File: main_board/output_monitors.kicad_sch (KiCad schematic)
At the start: 52 parts, among them U14 TL072CDR, U17 TL072CDR, U18 TL072CDR, U4 TL072CDR

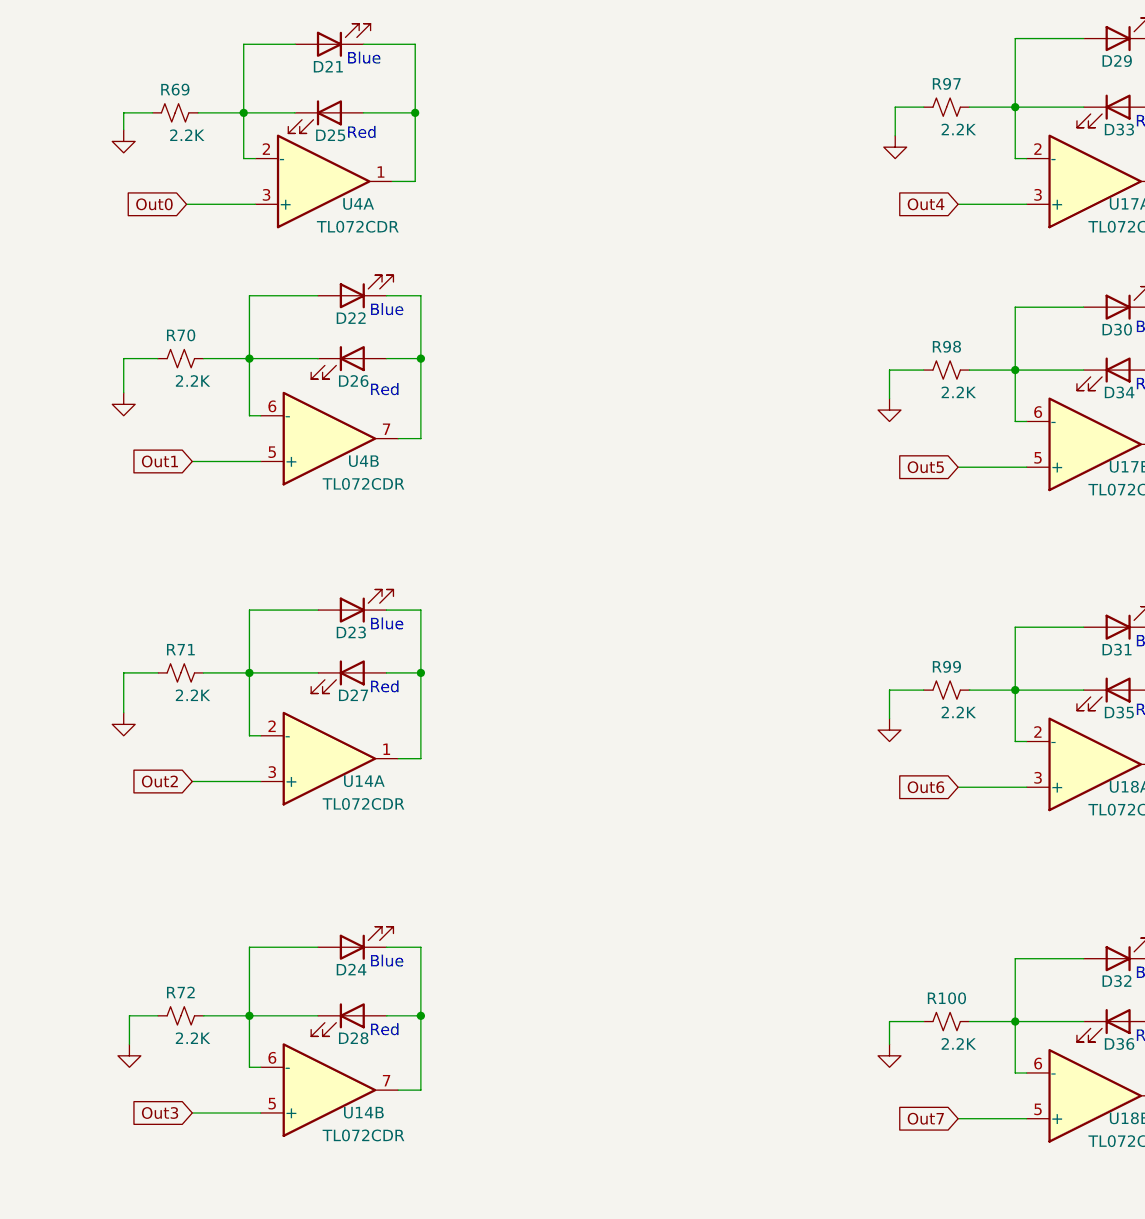
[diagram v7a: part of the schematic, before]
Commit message: Fixes main board.
Fixes regulator footprint. Re lays out board to improve noise performance. Around -50db now at outputs.
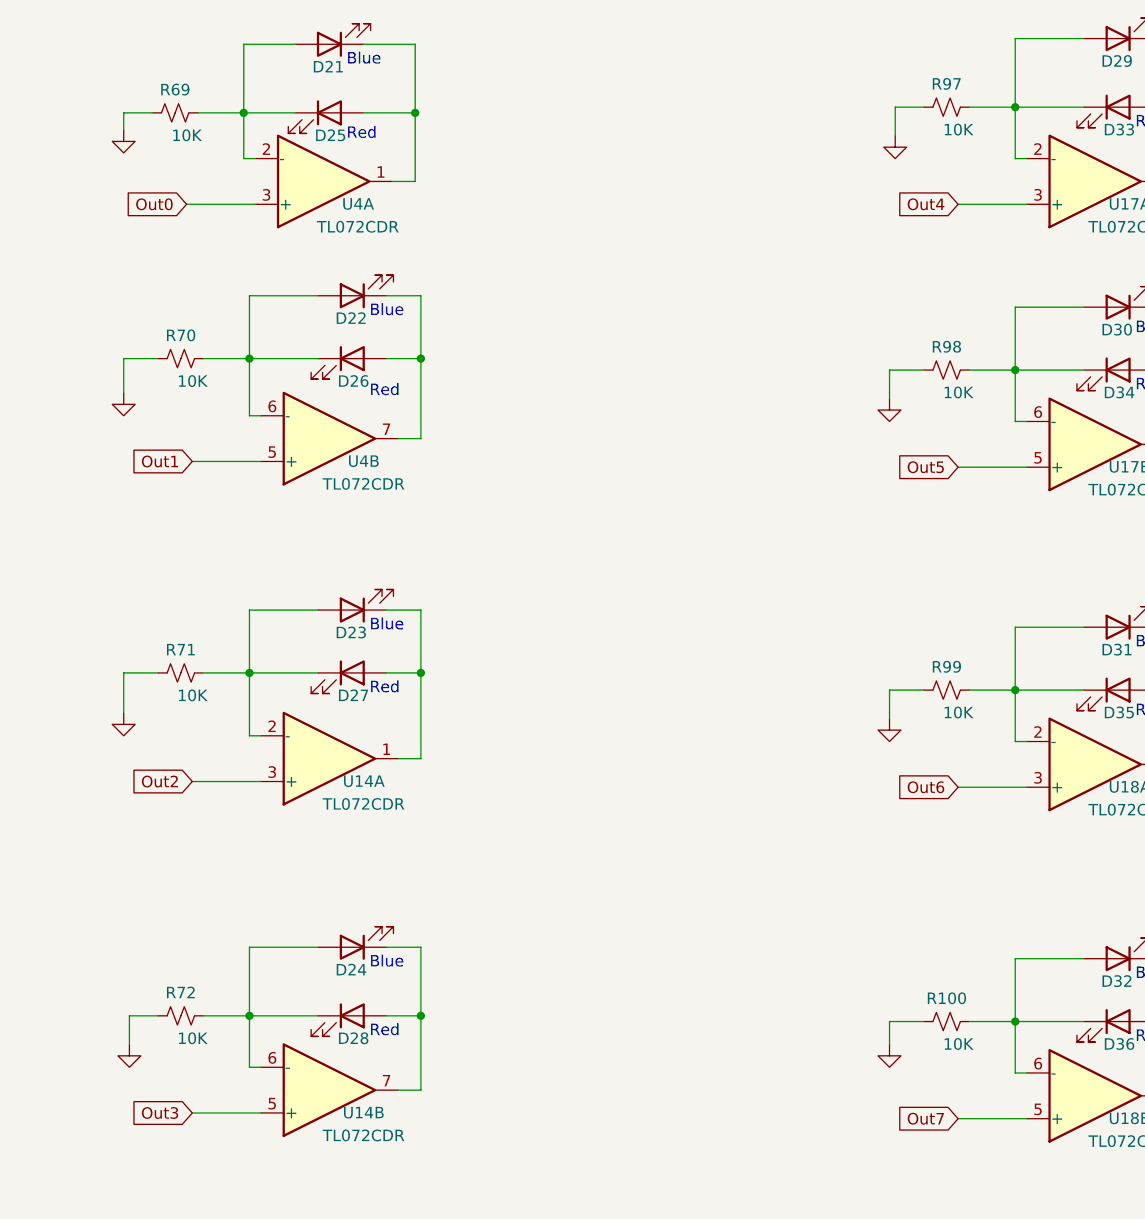
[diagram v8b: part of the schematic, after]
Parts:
- R100, R69, R70, R71, R72, R97, R98, R99: value 2.2K -> 10K; Digi-Key Part 311-10KARCT-ND -> 13-RC0805JR-1010KLCT-ND; LCSC Part # C17520 -> C17414
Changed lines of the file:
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@@
     (in_bom yes) (on_board yes)
     (property "Reference" "R72" (id 0) (at 79.375 125.095 90))
-    (property "Value" "2.2K" (id 1) (at 80.645 130.175 90))
+    (property "Value" "10K" (id 1) (at 80.645 130.175 90))
     (property "Footprint" "Resistor_SMD:R_0805_2012Metric_Pad1.20x1.40mm_HandSolder" (id 2) (at 79.375 127.635 0)
       (effects (font (size 1.27 1.27)) hide)
@@
       (effects (font (size 1.27 1.27)) hide)
     )
-    (property "Digi-Key Part" "311-10KARCT-ND" (id 4) (at 79.375 127.635 90)
-      (effects (font (size 1.27 1.27)) hide)
-    )
-    (property "LCSC Part #" "C17520" (id 5) (at 79.375 127.635 0)
+    (property "Digi-Key Part" "13-RC0805JR-1010KLCT-ND" (id 4) (at 79.375 127.635 90)
+      (effects (font (size 1.27 1.27)) hide)
+    )
+    (property "LCSC Part #" "C17414" (id 5) (at 79.375 127.635 0)
       (effects (font (size 1.27 1.27)) hide)
     )
@@
     (in_bom yes) (on_board yes)
     (property "Reference" "R100" (id 0) (at 164.465 125.73 90))
-    (property "Value" "2.2K" (id 1) (at 165.735 130.81 90))
+    (property "Value" "10K" (id 1) (at 165.735 130.81 90))
     (property "Footprint" "Resistor_SMD:R_0805_2012Metric_Pad1.20x1.40mm_HandSolder" (id 2) (at 164.465 128.27 0)
       (effects (font (size 1.27 1.27)) hide)
@@
       (effects (font (size 1.27 1.27)) hide)
     )
-    (property "Digi-Key Part" "311-10KARCT-ND" (id 4) (at 164.465 128.27 90)
-      (effects (font (size 1.27 1.27)) hide)
-    )
-    (property "LCSC Part #" "C17520" (id 5) (at 164.465 128.27 0)
+    (property "Digi-Key Part" "13-RC0805JR-1010KLCT-ND" (id 4) (at 164.465 128.27 90)
+      (effects (font (size 1.27 1.27)) hide)
+    )
+    (property "LCSC Part #" "C17414" (id 5) (at 164.465 128.27 0)
       (effects (font (size 1.27 1.27)) hide)
     )
@@
     (in_bom yes) (on_board yes)
     (property "Reference" "R69" (id 0) (at 78.74 24.765 90))
-    (property "Value" "2.2K" (id 1) (at 80.01 29.845 90))
+    (property "Value" "10K" (id 1) (at 80.01 29.845 90))
     (property "Footprint" "Resistor_SMD:R_0805_2012Metric_Pad1.20x1.40mm_HandSolder" (id 2) (at 78.74 27.305 0)
       (effects (font (size 1.27 1.27)) hide)
@@
       (effects (font (size 1.27 1.27)) hide)
     )
-    (property "Digi-Key Part" "311-10KARCT-ND" (id 4) (at 78.74 27.305 90)
-      (effects (font (size 1.27 1.27)) hide)
-    )
-    (property "LCSC Part #" "C17520" (id 5) (at 78.74 27.305 0)
+    (property "Digi-Key Part" "13-RC0805JR-1010KLCT-ND" (id 4) (at 78.74 27.305 90)
+      (effects (font (size 1.27 1.27)) hide)
+    )
+    (property "LCSC Part #" "C17414" (id 5) (at 78.74 27.305 0)
       (effects (font (size 1.27 1.27)) hide)
     )
@@
     (in_bom yes) (on_board yes)
     (property "Reference" "R99" (id 0) (at 164.465 88.9 90))
-    (property "Value" "2.2K" (id 1) (at 165.735 93.98 90))
+    (property "Value" "10K" (id 1) (at 165.735 93.98 90))
     (property "Footprint" "Resistor_SMD:R_0805_2012Metric_Pad1.20x1.40mm_HandSolder" (id 2) (at 164.465 91.44 0)
       (effects (font (size 1.27 1.27)) hide)
@@
       (effects (font (size 1.27 1.27)) hide)
     )
-    (property "Digi-Key Part" "311-10KARCT-ND" (id 4) (at 164.465 91.44 90)
-      (effects (font (size 1.27 1.27)) hide)
-    )
-    (property "LCSC Part #" "C17520" (id 5) (at 164.465 91.44 0)
+    (property "Digi-Key Part" "13-RC0805JR-1010KLCT-ND" (id 4) (at 164.465 91.44 90)
+      (effects (font (size 1.27 1.27)) hide)
+    )
+    (property "LCSC Part #" "C17414" (id 5) (at 164.465 91.44 0)
       (effects (font (size 1.27 1.27)) hide)
     )
@@
     (in_bom yes) (on_board yes)
     (property "Reference" "R98" (id 0) (at 164.465 53.34 90))
-    (property "Value" "2.2K" (id 1) (at 165.735 58.42 90))
+    (property "Value" "10K" (id 1) (at 165.735 58.42 90))
     (property "Footprint" "Resistor_SMD:R_0805_2012Metric_Pad1.20x1.40mm_HandSolder" (id 2) (at 164.465 55.88 0)
       (effects (font (size 1.27 1.27)) hide)
@@
       (effects (font (size 1.27 1.27)) hide)
     )
-    (property "Digi-Key Part" "311-10KARCT-ND" (id 4) (at 164.465 55.88 90)
-      (effects (font (size 1.27 1.27)) hide)
-    )
-    (property "LCSC Part #" "C17520" (id 5) (at 164.465 55.88 0)
+    (property "Digi-Key Part" "13-RC0805JR-1010KLCT-ND" (id 4) (at 164.465 55.88 90)
+      (effects (font (size 1.27 1.27)) hide)
+    )
+    (property "LCSC Part #" "C17414" (id 5) (at 164.465 55.88 0)
       (effects (font (size 1.27 1.27)) hide)
     )
@@
     (in_bom yes) (on_board yes)
     (property "Reference" "R70" (id 0) (at 79.375 52.07 90))
-    (property "Value" "2.2K" (id 1) (at 80.645 57.15 90))
+    (property "Value" "10K" (id 1) (at 80.645 57.15 90))
     (property "Footprint" "Resistor_SMD:R_0805_2012Metric_Pad1.20x1.40mm_HandSolder" (id 2) (at 79.375 54.61 0)
       (effects (font (size 1.27 1.27)) hide)
@@
       (effects (font (size 1.27 1.27)) hide)
     )
-    (property "Digi-Key Part" "311-10KARCT-ND" (id 4) (at 79.375 54.61 90)
-      (effects (font (size 1.27 1.27)) hide)
-    )
-    (property "LCSC Part #" "C17520" (id 5) (at 79.375 54.61 0)
+    (property "Digi-Key Part" "13-RC0805JR-1010KLCT-ND" (id 4) (at 79.375 54.61 90)
+      (effects (font (size 1.27 1.27)) hide)
+    )
+    (property "LCSC Part #" "C17414" (id 5) (at 79.375 54.61 0)
       (effects (font (size 1.27 1.27)) hide)
     )
@@
     (in_bom yes) (on_board yes)
     (property "Reference" "R71" (id 0) (at 79.375 86.995 90))
-    (property "Value" "2.2K" (id 1) (at 80.645 92.075 90))
+    (property "Value" "10K" (id 1) (at 80.645 92.075 90))
     (property "Footprint" "Resistor_SMD:R_0805_2012Metric_Pad1.20x1.40mm_HandSolder" (id 2) (at 79.375 89.535 0)
       (effects (font (size 1.27 1.27)) hide)
@@
       (effects (font (size 1.27 1.27)) hide)
     )
-    (property "Digi-Key Part" "311-10KARCT-ND" (id 4) (at 79.375 89.535 90)
-      (effects (font (size 1.27 1.27)) hide)
-    )
-    (property "LCSC Part #" "C17520" (id 5) (at 79.375 89.535 0)
+    (property "Digi-Key Part" "13-RC0805JR-1010KLCT-ND" (id 4) (at 79.375 89.535 90)
+      (effects (font (size 1.27 1.27)) hide)
+    )
+    (property "LCSC Part #" "C17414" (id 5) (at 79.375 89.535 0)
       (effects (font (size 1.27 1.27)) hide)
     )
@@
     (in_bom yes) (on_board yes)
     (property "Reference" "R97" (id 0) (at 164.465 24.13 90))
-    (property "Value" "2.2K" (id 1) (at 165.735 29.21 90))
+    (property "Value" "10K" (id 1) (at 165.735 29.21 90))
     (property "Footprint" "Resistor_SMD:R_0805_2012Metric_Pad1.20x1.40mm_HandSolder" (id 2) (at 164.465 26.67 0)
       (effects (font (size 1.27 1.27)) hide)
@@
       (effects (font (size 1.27 1.27)) hide)
     )
-    (property "Digi-Key Part" "311-10KARCT-ND" (id 4) (at 164.465 26.67 90)
-      (effects (font (size 1.27 1.27)) hide)
-    )
-    (property "LCSC Part #" "C17520" (id 5) (at 164.465 26.67 0)
-      (effects (font (size 1.27 1.27)) hide)
-    )
+    (property "Digi-Key Part" "13-RC0805JR-1010KLCT-ND" (id 4) (at 164.465 26.67 90)
+      (effects (font (size 1.27 1.27)) hide)
+    )
+    (property "LCSC Part #" "C17414" (id 5) (at 164.465 26.67 0)
+      (effects (font (size 1.27 1.27)) hide)
+    )
